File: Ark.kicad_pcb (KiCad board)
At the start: 2 copper layers, 108 parts, among them P1 USB_OTG, P2 USB_OTG, P3 40_Pin_LCD_Out, Q1 MMUN2133LT1G, SW1 SW_PUSH_SMALL_H, SW2 SW_PUSH_SMALL_H, SW3 SW_PUSH_SMALL_H, SW4 SW_PUSH_SMALL_H, SW5 SW_PUSH_SMALL_H, SW6 SW_PUSH_SMALL_H, U1 PAM2306AYPKE, U2 AP7115-25SEG, U3 DDR2_SODIMM_CM_3_Lite, U4 1040310811, U5 FAN5333BSX, U6 TPS61090RSAR, U7 MCP73871, U8 SPDT_switch

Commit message: Updated PCB design
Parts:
- D3, D4, D5, D6, SW1, SW2, SW3, SW4, SW5, SW6: moved to B.Cu
- moved C10 151.0 mm to (113.4, 97.9)
- moved SW5 143.6 mm to (166.1, 153.5)
- moved C8 141.6 mm to (106.5, 100.6)
- moved C9 141.6 mm to (114.3, 100.7)
- moved SW1 140.0 mm to (139.7, 149.1), turned to 315 degrees
- moved D4 129.0 mm to (133.6, 164.6)
- moved D3 126.8 mm to (127.8, 164.6)
- moved SW4 126.0 mm to (151.1, 153.5)
- moved P2 122.9 mm to (115.6, 163.6)
- moved D5 122.7 mm to (153.0, 164.6)
- moved D6 122.2 mm to (162.7, 164.3)
- moved SW3 121.9 mm to (128.3, 153.5)
- moved L2 121.8 mm to (110.6, 84.8), turned to 90 degrees
- moved C7 120.2 mm to (125.2, 94.5)
- moved C17 119.8 mm to (113.5, 155.5), turned to 90 degrees
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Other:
- board outline added: 71.9 x 88.3 mm

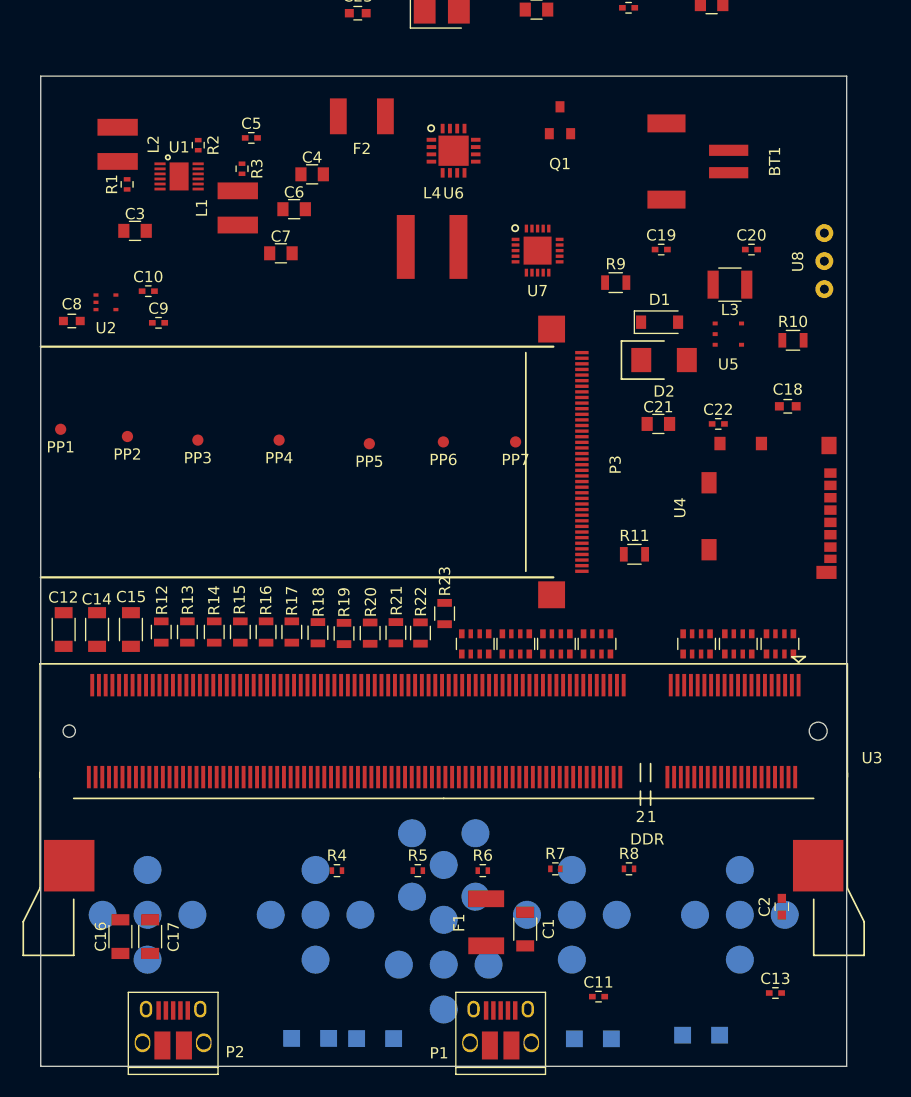
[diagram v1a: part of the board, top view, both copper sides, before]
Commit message: Added touch interface and aligned ribbon cables
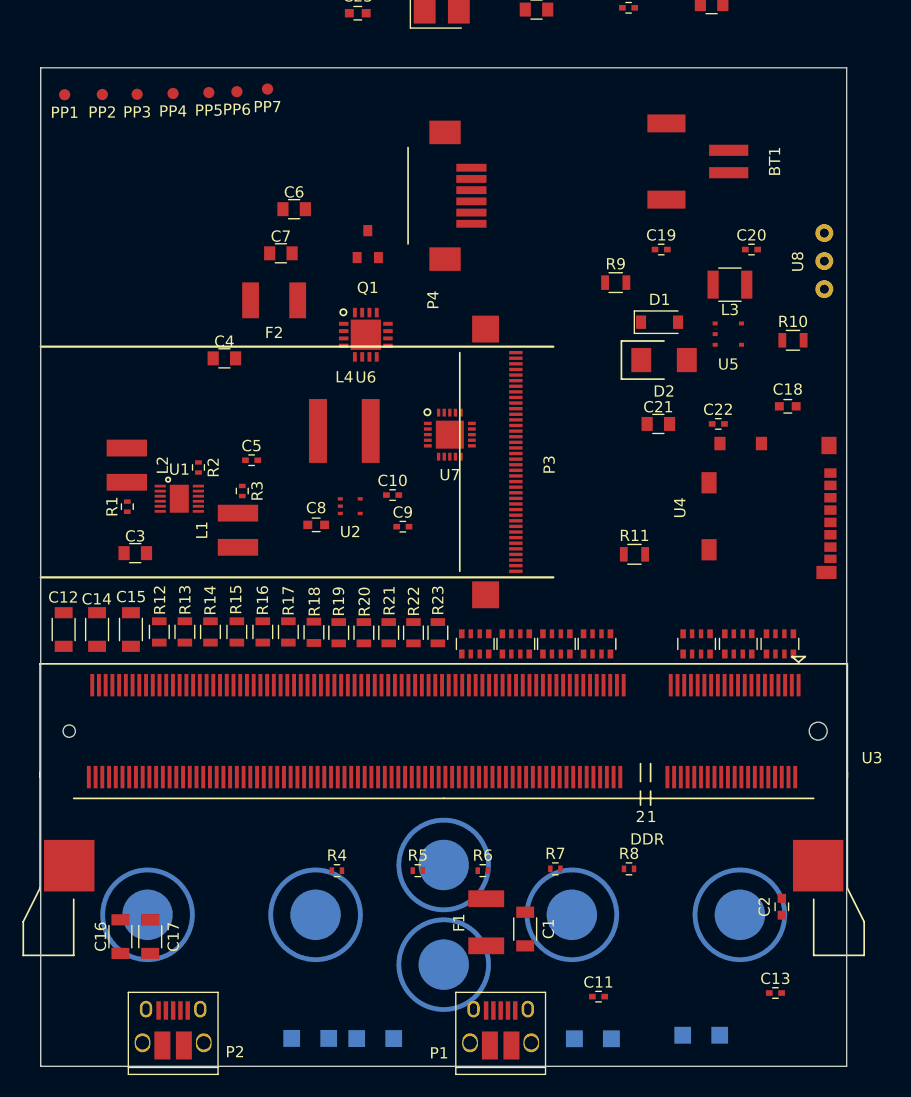
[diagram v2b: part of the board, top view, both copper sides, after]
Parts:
- added P4: 6_Pin_Touch_In, Pi-Library:Touch_Molex_Connector, F.Cu at (142.2, 89.4)
- moved PP7 38.5 mm to (124.0, 79.9)
- moved PP6 36.3 mm to (121.3, 80.1)
- moved PP5 34.4 mm to (118.8, 80.2)
- moved PP4 32.3 mm to (115.6, 80.3)
- moved PP3 31.3 mm to (112.4, 80.4)
- moved PP2 30.6 mm to (109.3, 80.4)
- moved PP1 29.8 mm to (105.9, 80.4)
- moved L1 28.7 mm to (121.4, 119.2)
- moved R3 28.7 mm to (121.7, 115.7)
- moved U1 28.7 mm to (116.1, 116.4)
- moved C3 28.7 mm to (112.2, 121.3)
- moved C5 28.7 mm to (122.6, 113.0)
- moved R1 28.7 mm to (111.5, 117.1)
- moved R2 28.7 mm to (117.8, 113.6)
- moved L2 28.6 mm to (111.4, 113.4)
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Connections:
- net HOME renamed Net-(U3-Pad36)
- net L_BUMP renamed Net-(U3-Pad58)
- net Net-(R6-Pad1) renamed SCL
- net Net-(R7-Pad1) renamed SDA
- net SELECT renamed Net-(U3-Pad60)
- net START renamed Net-(U3-Pad64)
- net X renamed Net-(U3-Pad72)
- U3 pad 76: Y -> INT
- U3 pad 78: R_BUMP -> RESET
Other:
- board size 71.9 x 88.3 mm -> 71.9 x 89.1 mm

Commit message: Components placed
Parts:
- moved R30 48.1 mm to (167.7, 88.4)
- moved R31 47.5 mm to (168.7, 94.4), turned to 90 degrees
- moved R32 40.8 mm to (168.6, 91.3), turned to 90 degrees
- moved Q1 34.8 mm to (166.5, 84.4), turned to 90 degrees
- moved U6 32.5 mm to (163.8, 92.5)
- moved C23 32.0 mm to (162.3, 83.5)
- moved R29 31.4 mm to (154.2, 81.7), turned to 180 degrees
- moved L4 31.2 mm to (156.6, 92.8), turned to 0 degrees
- moved C6 31.0 mm to (114.1, 119.0), turned to 180 degrees
- moved C25 30.2 mm to (164.8, 97.8), turned to 270 degrees
- moved R28 30.0 mm to (150.9, 81.7)
- moved R27 27.9 mm to (164.5, 88.4)
- moved R26 27.6 mm to (155.8, 87.9), turned to 270 degrees
- moved C20 27.5 mm to (150.1, 115.8), turned to 180 degrees
- moved U7 27.4 mm to (152.3, 86.1), turned to 180 degrees
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
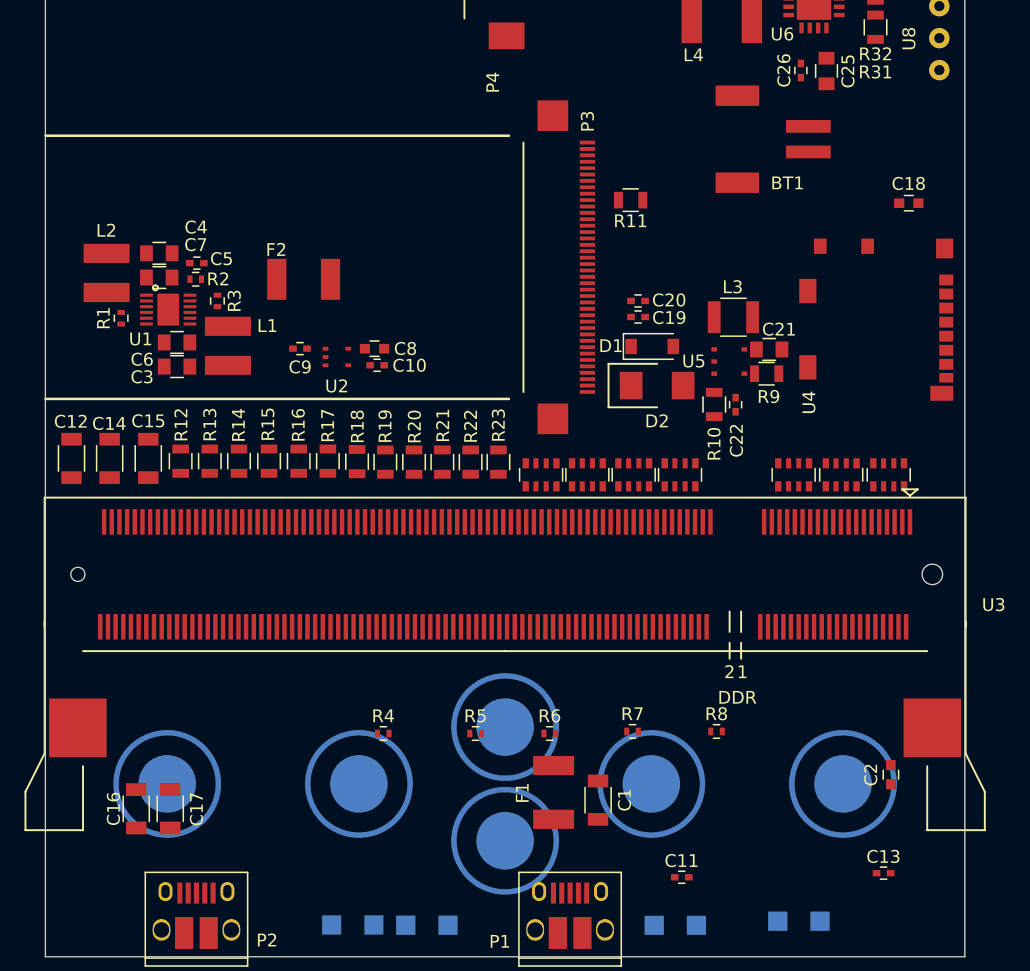
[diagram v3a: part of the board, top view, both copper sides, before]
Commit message: Data tracks layed down
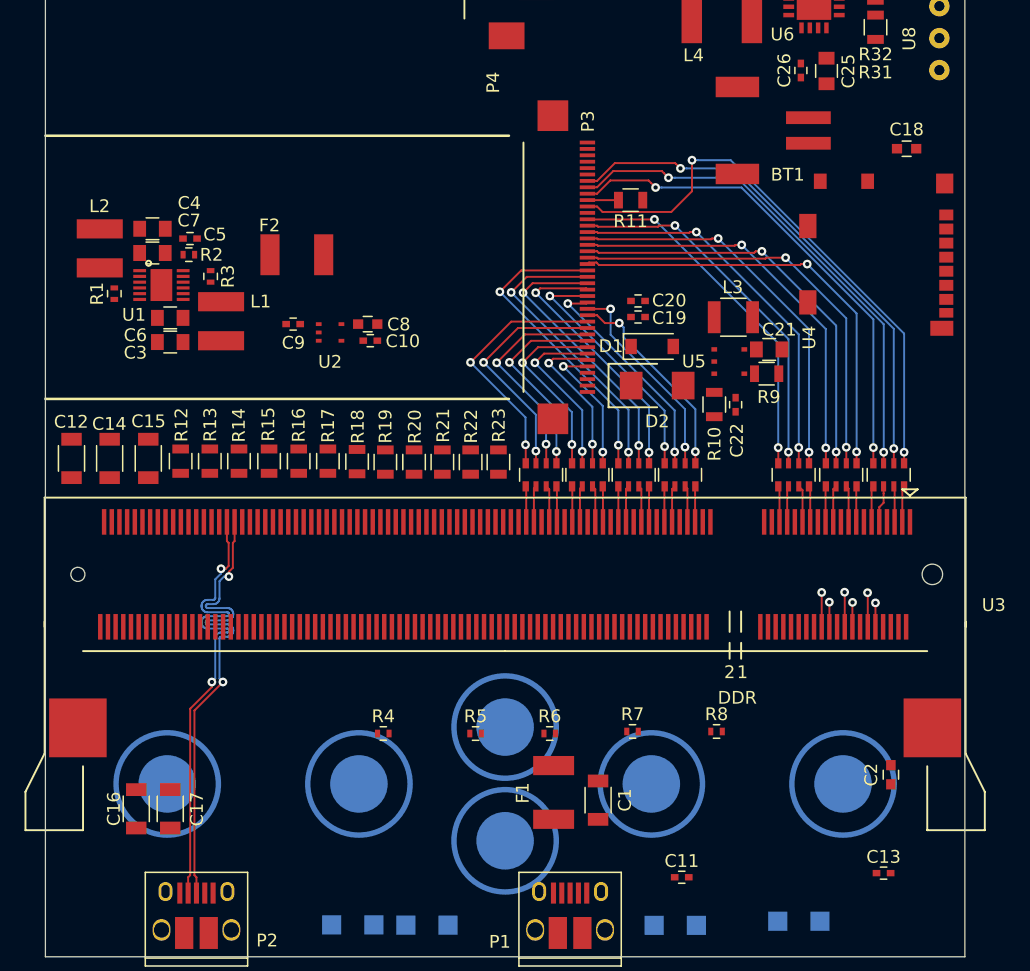
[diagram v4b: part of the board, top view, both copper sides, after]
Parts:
- moved U4 5.08 mm to (174.2, 112.2)
- moved C18 4.26 mm to (171.1, 103.9)
- moved C10 1.99 mm to (129.2, 118.9)
- moved C3 1.99 mm to (113.5, 119.0)
- moved C5 1.99 mm to (115.1, 110.9)
- moved C6 1.99 mm to (113.5, 117.1)
- moved C8 1.99 mm to (129.0, 117.6)
- moved F2 1.99 mm to (123.4, 112.2)
- moved L1 1.99 mm to (117.5, 117.4)
- moved R1 1.99 mm to (109.1, 115.2)
- moved U2 1.99 mm to (126.0, 118.2)
- moved C4 1.99 mm to (112.1, 110.1)
- moved C7 1.99 mm to (112.1, 112.0)
- moved C9 1.99 mm to (123.1, 117.6)
- moved L2 1.99 mm to (108.0, 111.7)
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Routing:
- net Net-(P3-Pad30): track 0.00 -> 43.8 mm, vias 0 -> 2
- net Net-(P3-Pad34): track 0.00 -> 40.4 mm, vias 0 -> 2
- net Net-(P3-Pad33): track 0.00 -> 39.5 mm, vias 0 -> 2
- net Net-(P3-Pad32): track 0.00 -> 38.5 mm, vias 0 -> 2
- net USB_D+: track 0.00 -> 38.1 mm, vias 0 -> 2
- net USB_D-: track 0.00 -> 37.9 mm, vias 0 -> 2
- net Net-(P3-Pad21): track 0.00 -> 34.5 mm, vias 0 -> 2
- net Net-(P3-Pad22): track 0.00 -> 33.6 mm, vias 0 -> 2
- net Net-(P3-Pad23): track 0.00 -> 32.7 mm, vias 0 -> 2
- net Net-(P3-Pad24): track 0.00 -> 31.9 mm, vias 0 -> 2
- net Net-(P3-Pad25): track 0.00 -> 30.8 mm, vias 0 -> 2
- net Net-(P3-Pad26): track 0.00 -> 30.0 mm, vias 0 -> 2
- net Net-(P3-Pad27): track 0.00 -> 29.2 mm, vias 0 -> 2
- net Net-(P3-Pad28): track 0.00 -> 28.3 mm, vias 0 -> 2
- net Net-(P3-Pad20): track 0.00 -> 24.8 mm, vias 0 -> 2
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
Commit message: Nearly finished traces
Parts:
- moved R4 32.5 mm to (162.7, 147.7), turned to 270 degrees
- moved R5 26.2 mm to (163.3, 145.5), turned to 270 degrees
- moved D4 21.4 mm to (155.0, 164.3)
- moved D5 18.9 mm to (134.1, 164.3)
- moved C13 17.1 mm to (159.7, 146.4), turned to 270 degrees
- moved R8 15.1 mm to (141.7, 145.5), turned to 270 degrees
- moved C11 14.6 mm to (155.5, 146.4), turned to 270 degrees
- moved R7 7.28 mm to (143.5, 145.6), turned to 270 degrees
- moved R6 1.86 mm to (142.9, 147.8), turned to 270 degrees
- moved C1 1.21 mm to (147.0, 153.6), turned to 270 degrees
- moved D3 0.23 mm to (127.8, 164.3)
- moved D6 0.06 mm to (162.7, 164.3)
- moved L2 0.05 mm to (108.0, 111.7)
- turned F1 to 270 degrees
- turned SW1 to 0 degrees
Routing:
- net 3V3: track 0.00 -> 396.8 mm, vias 0 -> 10
- net 1V8: track 0.00 -> 114.5 mm, vias 0 -> 2
- net 5V: track 0.00 -> 114.5 mm, vias 0 -> 6
- net PWR_IN: track 0.00 -> 84.5 mm, vias 0 -> 2
- net CM_VDAC: track 0.00 -> 80.6 mm, vias 0 -> 4
- net SDA: track 0.00 -> 69.2 mm, vias 0 -> 4
- net INT: track 0.00 -> 68.4 mm, vias 0 -> 4
- net RESET: track 0.00 -> 67.0 mm, vias 0 -> 2
- net SCL: track 0.00 -> 66.5 mm, vias 0 -> 2
- net 24V: track 0.00 -> 63.3 mm, vias 0 -> 2
- net Net-(BT1-Pad1): track 0.00 -> 59.4 mm, vias 0 -> 2
- net Net-(C23-Pad1): track 0.00 -> 56.6 mm, vias 0 -> 4
- net A_IN: track 0.00 -> 54.4 mm, vias 0 -> 3
- net UP: track 0.00 -> 49.8 mm, vias 0 -> 4
- net DOWN: track 0.00 -> 45.7 mm, vias 0 -> 2
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- added copper zone on F.Cu, net 1V8
- added copper zone on F.Cu, net 3V3
- added copper zone on F.Cu, net 5V
- added copper zone on F.Cu, net GND
- added copper zone on F.Cu, net Net-(BT1-Pad1)
- added copper zone on F.Cu, net Net-(C23-Pad1)
- added copper zone on F.Cu, net PWR_IN
- added copper zone on F.Cu, net VBAT
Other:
- board text added: "Charged"
- board text added: "Charging"
- board text added: "Low Battery"
- board text added: "On"
- board text added: "The Ark"

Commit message: Completed the PCB design
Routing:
- net Net-(D4-Pad1): track 0.00 -> 156.9 mm, vias 0 -> 3
- net Net-(D3-Pad2): track 0.00 -> 145.6 mm, vias 0 -> 3
- net Net-(D5-Pad1): track 0.00 -> 142.6 mm, vias 0 -> 3
- net Net-(D6-Pad2): track 0.00 -> 93.8 mm, vias 0 -> 1
- net GND: track 3.59 -> 90.2 mm, vias 0 -> 18
- net PWR_IN: track 84.5 -> 134.8 mm, vias 2 -> 7
- net 5V: track 114.5 -> 159.3 mm, vias 6 -> 10
- net Net-(L4-Pad2): track 0.00 -> 3.80 mm
- net SDA: track 69.2 -> 72.7 mm
- net SCL: track 66.5 -> 69.0 mm
- added copper zone on B.Cu, net GND
- added copper zone on F.Cu, net Net-(L4-Pad2)

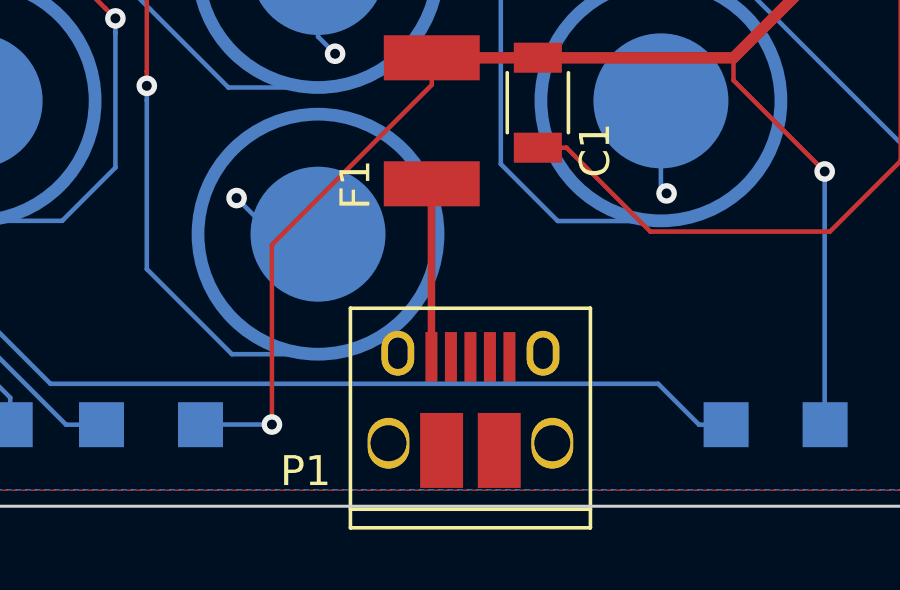
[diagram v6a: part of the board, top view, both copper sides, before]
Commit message: Fixed USB problem
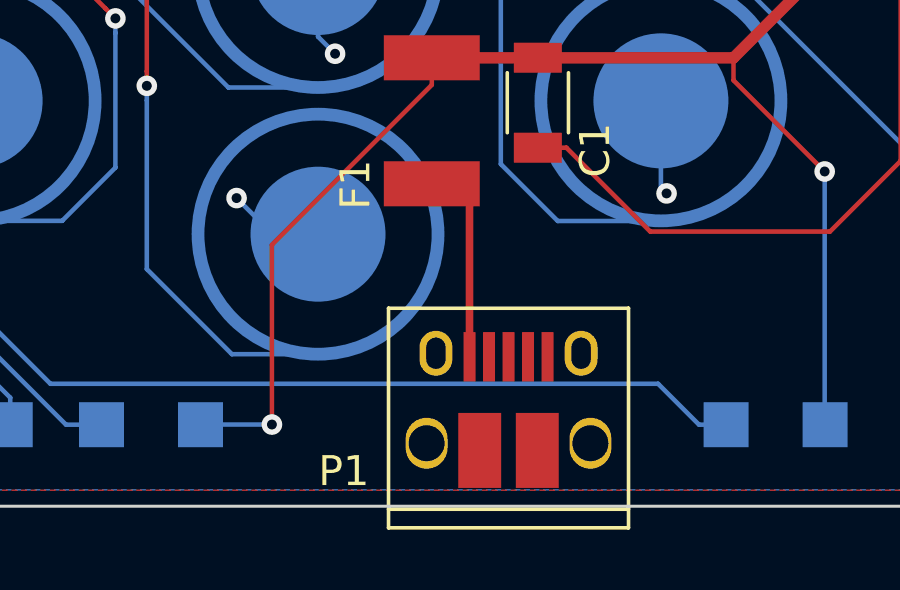
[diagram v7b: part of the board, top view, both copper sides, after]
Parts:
- moved P1 1.27 mm to (146.1, 163.6)
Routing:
- net Net-(F1-Pad2): track 5.77 -> 6.82 mm
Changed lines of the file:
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@@
     (thickness 1.6002)
     (drawings 12)
-    (tracks 1412)
+    (tracks 1414)
     (zones 0)
     (modules 109)
@@
   )
   (module Pi-Library:USB_Micro-B_10103594-0001LF (layer F.Cu)
-    (at 144.78 163.576)
+    (at 146.05 163.576)
     (descr "Micro USB Type B 10103594-0001LF")
     (tags "USB USB_B USB_micro USB_OTG")
@@
   (segment (start 171.03344 81.7118) (end 172.07484 82.7532) (width 0.1524) (layer F.Cu) (net 18))
   (via (at 172.07484 82.7532) (size 0.6858) (drill 0.3302) (layers F.Cu B.Cu) (net 18))
-  (segment (start 143.48 162.076) (end 143.48 156.3207) (width 0.254) (layer F.Cu) (net 19))
+  (segment (start 144.75 162.076) (end 144.75 156.688) (width 0.254) (layer F.Cu) (net 19))
+  (segment (start 144.75 156.688) (end 144.37048 156.30848) (width 0.254) (layer F.Cu) (net 19))
+  (segment (start 144.37048 156.30848) (end 143.49222 156.30848) (width 0.254) (layer F.Cu) (net 19))
   (segment (start 143.48 156.3207) (end 143.49222 156.30848) (width 0.254) (layer F.Cu) (net 19))
   (segment (start 114.52934 115.2163) (end 116.11546 115.2163) (width 0.254) (layer F.Cu) (net 20))
